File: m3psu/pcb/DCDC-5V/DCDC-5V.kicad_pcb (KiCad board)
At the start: 2 copper layers, 39.5 x 39.5 mm, 52 parts, among them IC1 LTC2975, IC2 TPS62133, IC3 TPS62152, J1 WEST TOP, J2 WEST BOT, J3 NORTH TOP, J4 EAST TOP, J5 EAST BOT, J6 NORTH BOT, Q1 NFET_GDS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

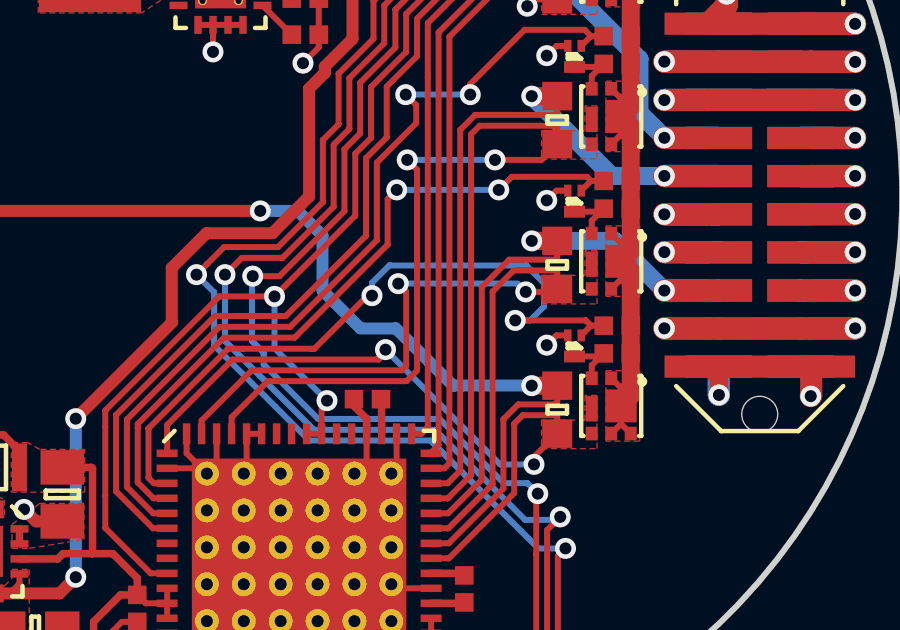
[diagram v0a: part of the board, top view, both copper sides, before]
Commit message: Small routing optimisation to DCDC-5V board
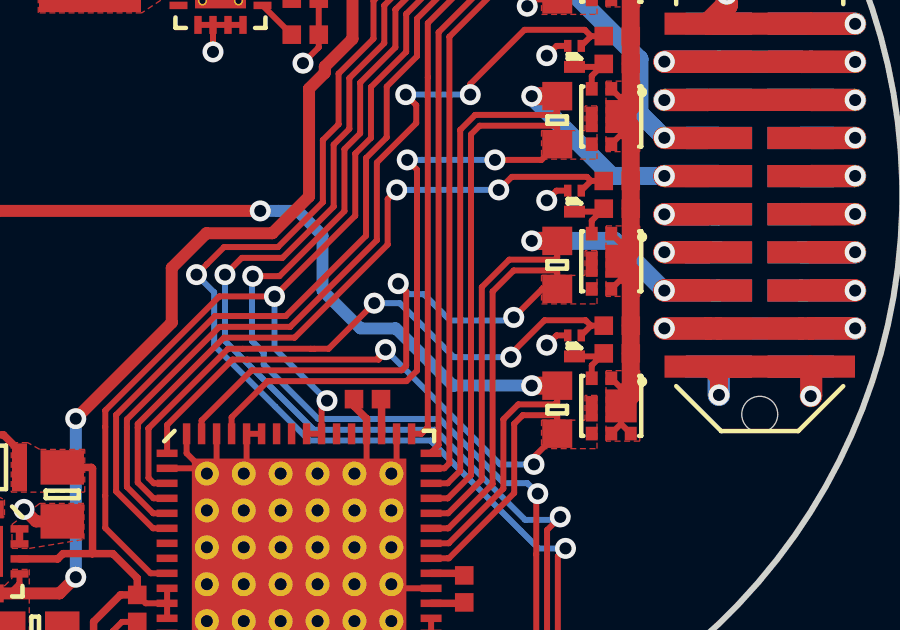
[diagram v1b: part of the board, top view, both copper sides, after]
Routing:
- net /VEN_0: track 23.7 -> 21.1 mm
- net /ISNS1+: track 28.4 -> 29.4 mm
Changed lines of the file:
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@@
     (thickness 1.6)
     (drawings 5)
-    (tracks 867)
+    (tracks 868)
     (zones 0)
     (modules 52)
@@
   )
   (setup
-    (last_trace_width 0.25)
+    (last_trace_width 0.2)
     (user_trace_width 0.16)
     (user_trace_width 0.2)
@@
   (segment (start 104.640655 112.105) (end 104.595 112.105) (width 0.2) (layer F.Cu) (net 41))
   (segment (start 104.595 112.105) (end 104.045 112.105) (width 0.2) (layer F.Cu) (net 41))
-  (segment (start 102.075 103.35) (end 102.075 102.922198) (width 0.2) (layer B.Cu) (net 42))
-  (segment (start 102.075 102.922198) (end 102.657199 102.339999) (width 0.2) (layer B.Cu) (net 42))
-  (segment (start 102.657199 102.339999) (end 107.217801 102.339999) (width 0.2) (layer B.Cu) (net 42))
-  (segment (start 107.217801 102.339999) (end 107.810001 102.932199) (width 0.2) (layer B.Cu) (net 42))
-  (segment (start 107.810001 102.932199) (end 107.810001 103.709973) (width 0.2) (layer B.Cu) (net 42))
-  (segment (start 107.810001 103.709973) (end 107.344974 104.175) (width 0.2) (layer B.Cu) (net 42))
-  (segment (start 107.344974 104.175) (end 106.85 104.175) (width 0.2) (layer B.Cu) (net 42))
+  (segment (start 103 103.6) (end 104.8 105.4) (width 0.2) (layer B.Cu) (net 42))
+  (segment (start 104.8 105.4) (end 106.705041 105.4) (width 0.2) (layer B.Cu) (net 42))
+  (segment (start 102.15 103.6) (end 103 103.6) (width 0.2) (layer B.Cu) (net 42))
+  (segment (start 100.15503 105.11997) (end 100.63003 105.11997) (width 0.2) (layer F.Cu) (net 42))
+  (segment (start 100.63003 105.11997) (end 102.15 103.6) (width 0.2) (layer F.Cu) (net 42))
+  (via (at 102.15 103.6) (size 0.7) (drill 0.4) (layers F.Cu B.Cu) (net 42))
+  (segment (start 109.195301 104.170301) (end 107.826897 104.170301) (width 0.2) (layer F.Cu) (net 42))
+  (segment (start 107.826897 104.170301) (end 106.705041 105.292157) (width 0.2) (layer F.Cu) (net 42))
+  (segment (start 106.705041 105.292157) (end 106.705041 105.4) (width 0.2) (layer F.Cu) (net 42))
+  (via (at 106.705041 105.4) (size 0.7) (drill 0.4) (layers F.Cu B.Cu) (net 42))
+  (segment (start 94.801998 109.605) (end 94.625 109.428002) (width 0.2) (layer F.Cu) (net 42))
+  (segment (start 95.245 109.605) (end 94.801998 109.605) (width 0.2) (layer F.Cu) (net 42))
+  (segment (start 94.625 109.428002) (end 94.625 107.775) (width 0.2) (layer F.Cu) (net 42))
+  (segment (start 97.277897 105.11997) (end 97.768766 105.11997) (width 0.2) (layer F.Cu) (net 42))
+  (segment (start 94.625 107.772867) (end 97.277897 105.11997) (width 0.2) (layer F.Cu) (net 42))
+  (segment (start 94.625 107.775) (end 94.625 107.772867) (width 0.2) (layer F.Cu) (net 42))
+  (segment (start 97.768766 105.11997) (end 100.03003 105.11997) (width 0.2) (layer F.Cu) (net 42))
   (segment (start 100.03003 105.11997) (end 100.15503 105.11997) (width 0.2) (layer F.Cu) (net 42))
-  (segment (start 100.15503 105.11997) (end 101.925 103.35) (width 0.2) (layer F.Cu) (net 42))
-  (segment (start 101.925 103.35) (end 102.075 103.35) (width 0.2) (layer F.Cu) (net 42))
-  (via (at 102.075 103.35) (size 0.7) (drill 0.4) (layers F.Cu B.Cu) (net 42))
   (segment (start 109.195301 104.170301) (end 109.190602 104.175) (width 0.2) (layer F.Cu) (net 42))
-  (segment (start 109.190602 104.175) (end 106.85 104.175) (width 0.2) (layer F.Cu) (net 42))
-  (segment (start 97.768766 105.11997) (end 100.03003 105.11997) (width 0.2) (layer F.Cu) (net 42))
-  (segment (start 94.625 107.775) (end 94.625 107.772867) (width 0.2) (layer F.Cu) (net 42))
-  (segment (start 94.625 107.772867) (end 97.277897 105.11997) (width 0.2) (layer F.Cu) (net 42))
-  (segment (start 97.277897 105.11997) (end 97.768766 105.11997) (width 0.2) (layer F.Cu) (net 42))
   (segment (start 109.375 104.35) (end 109.195301 104.170301) (width 0.2) (layer F.Cu) (net 42))
-  (segment (start 106.854699 104.170301) (end 106.85 104.175) (width 0.2) (layer F.Cu) (net 42))
-  (via (at 106.85 104.175) (size 0.7) (drill 0.4) (layers F.Cu B.Cu) (net 42))
   (segment (start 109.8 104.35) (end 109.375 104.35) (width 0.2) (layer F.Cu) (net 42))
   (segment (start 109.375 104.35) (end 109.05 104.675) (width 0.2) (layer F.Cu) (net 42))
-  (segment (start 94.625 109.428002) (end 94.625 107.775) (width 0.2) (layer F.Cu) (net 42))
-  (segment (start 95.245 109.605) (end 94.801998 109.605) (width 0.2) (layer F.Cu) (net 42))
-  (segment (start 94.801998 109.605) (end 94.625 109.428002) (width 0.2) (layer F.Cu) (net 42))
   (segment (start 109.239999 99.389999) (end 106.735001 99.389999) (width 0.2) (layer F.Cu) (net 43))
   (segment (start 102.9 99.825) (end 103.394974 99.825) (width 0.2) (layer B.Cu) (net 43))
@@
   (segment (start 104.045 112.605) (end 105.08 112.605) (width 0.25) (layer F.Cu) (net 52))
   (segment (start 105.08 112.605) (end 105.15 112.675) (width 0.25) (layer F.Cu) (net 52))
-  (segment (start 107.2 103.225) (end 108.15 103.225) (width 0.2) (layer F.Cu) (net 53))
+  (segment (start 108.25 103.125) (end 107.75 103.125) (width 0.2) (layer F.Cu) (net 53))
+  (segment (start 107.75 103.125) (end 106.8 104.075) (width 0.2) (layer F.Cu) (net 53))
+  (segment (start 104.675 104.175) (end 106.7 104.175) (width 0.2) (layer B.Cu) (net 53))
+  (segment (start 106.7 104.175) (end 106.8 104.075) (width 0.2) (layer B.Cu) (net 53))
+  (via (at 106.8 104.075) (size 0.7) (drill 0.4) (layers F.Cu B.Cu) (net 53))
+  (segment (start 103.799999 103.299999) (end 104.675 104.175) (width 0.2) (layer B.Cu) (net 53))
+  (segment (start 102.95 102.95) (end 103.299999 103.299999) (width 0.2) (layer B.Cu) (net 53))
+  (segment (start 103.299999 103.299999) (end 103.799999 103.299999) (width 0.2) (layer B.Cu) (net 53))
   (segment (start 108.15 103.225) (end 108.25 103.125) (width 0.2) (layer F.Cu) (net 53))
-  (segment (start 102.95 102.95) (end 106.925 102.95) (width 0.2) (layer B.Cu) (net 53))
-  (segment (start 106.925 102.95) (end 107.2 103.225) (width 0.2) (layer B.Cu) (net 53))
-  (via (at 107.2 103.225) (size 0.7) (drill 0.4) (layers F.Cu B.Cu) (net 53))
   (segment (start 103.214961 105.685039) (end 103.214961 103.214961) (width 0.2) (layer F.Cu) (net 53))
   (segment (start 103.214961 103.214961) (end 102.95 102.95) (width 0.2) (layer F.Cu) (net 53))

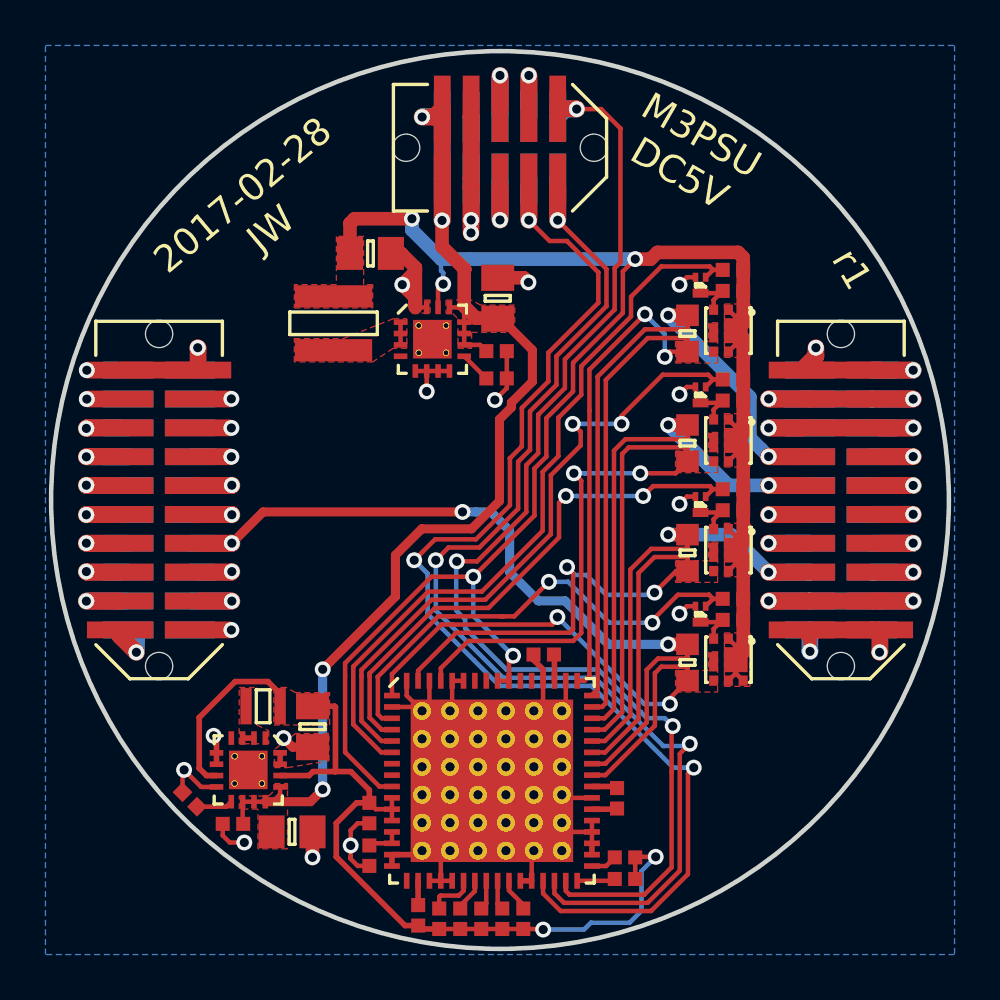
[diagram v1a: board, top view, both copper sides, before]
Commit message: Update NFET footprint on 5v board, add pull-downs
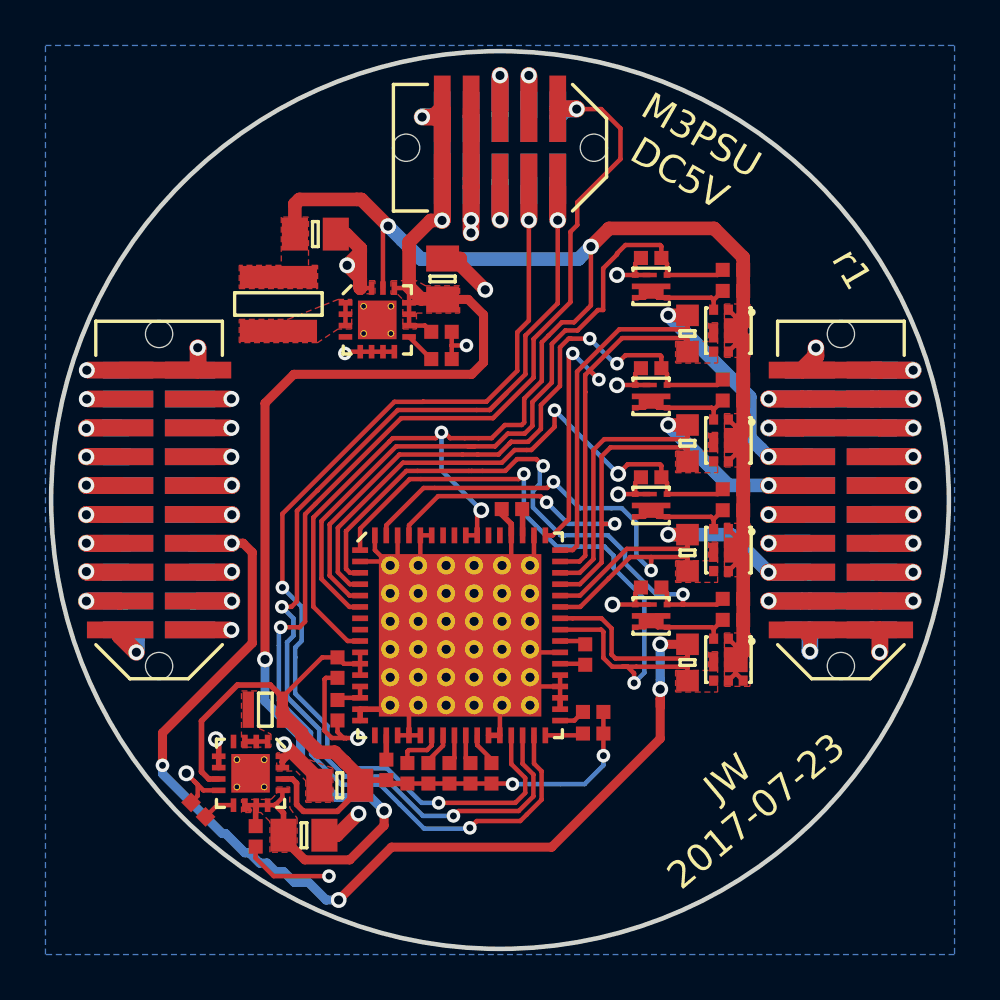
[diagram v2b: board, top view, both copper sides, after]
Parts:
- added R21: 1M, agg:0402, F.Cu at (106.7, 103.8)
- added R22: 1M, agg:0402, F.Cu at (106.7, 99.0)
- added R23: 1M, agg:0402, F.Cu at (106.7, 94.2)
- added R24: 1M, agg:0402, F.Cu at (106.7, 89.3)
- Q1, Q2, Q3, Q4: footprint agg:SOT-883-B -> agg:PowerPAK-SC-75-6L-Single
- moved G*** 35.0 mm to (65.0, 104.5)
- moved C1 6.55 mm to (92.8, 107.4)
- moved C3 6.55 mm to (92.8, 109.2)
- moved R1 6.55 mm to (95.0, 111.9)
- moved IC1 6.55 mm to (98.2, 106.0)
- moved R3 6.55 mm to (104.1, 109.3)
- moved R4 6.55 mm to (96.8, 112.0)
- moved R5 6.55 mm to (104.1, 110.3)
- moved R6 6.55 mm to (95.9, 112.0)
- moved R8 6.55 mm to (99.6, 112.0)
- moved C2 6.55 mm to (100.5, 100.4)
- moved R2 6.55 mm to (98.7, 112.0)
- moved R7 6.55 mm to (97.8, 112.0)
- moved C4 6.48 mm to (103.8, 106.8)
- moved C12 2.84 mm to (93.0, 112.5), turned to 180 degrees
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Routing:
- net /5v_CAN: track 35.5 -> 56.2 mm, vias 3 -> 5
- net /ISNS3+: track 40.7 -> 25.8 mm
- net VCC: track 54.5 -> 68.5 mm
- net /ISNS2+: track 36.3 -> 22.5 mm
- net GND: track 81.8 -> 95.4 mm
- net /SDA: track 54.2 -> 47.1 mm
- net /ISNS1+: track 29.4 -> 23.2 mm
- net /VEN_0: track 21.1 -> 27.0 mm
- net /ISNS0+: track 25.3 -> 30.5 mm
- net /5v_IMU: track 26.2 -> 21.1 mm
- net /5v_CAM: track 21.3 -> 16.3 mm
- net /5v_RADIO: track 31.7 -> 26.9 mm
- net 3v3: track 42.2 -> 37.6 mm
- net Net-(Q2-PadD): track 2.01 -> 6.45 mm
- net Net-(Q4-PadD): track 2.01 -> 6.44 mm
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- removed copper zone on F.Cu, net 3v3
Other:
- board text added: "JW 2017-07-23"
- board text removed: "2017-02-28 JW"

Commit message: Fix silkscreen, add test pads
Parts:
- added TP1: TESTPAD, agg:TESTPAD, F.Cu at (100.2, 91.6)
- added TP2: TESTPAD, agg:TESTPAD, F.Cu at (101.7, 90.3)
- added TP3: TESTPAD, agg:TESTPAD, F.Cu at (106.5, 86.8)
- added TP4: TESTPAD, agg:TESTPAD, F.Cu at (112.5, 90.2)
- C12, C8, C9: value 22µ -> 22u
- C5: value 10µ -> 10u
- L1: value 2µ2 -> 2u2
- L2: value 3µ3 -> 3u3
- moved G*** 35.2 mm to (99.9, 100.3)
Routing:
- net /~ALERT: track 57.0 -> 58.8 mm
- net GND: track 95.4 -> 96.6 mm, vias 24 -> 25
- net /SDA: track 47.1 -> 48.3 mm
- net /SCL: track 50.1 -> 51.0 mm
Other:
- board text added: "JW 2017-07-25"
- board text removed: "JW 2017-07-23"

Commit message: Add additional decoupling capacitor to 5V board
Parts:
- added C13: 22u, agg:0805, F.Cu at (111.6, 110.2)
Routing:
- net /V_DIST: track 89.8 -> 93.1 mm
- net GND: track 96.6 -> 95.5 mm, vias 25 -> 26
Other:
- board text added: "JW 2017-07-26"
- board text removed: "JW 2017-07-25"
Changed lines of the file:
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@@
 (kicad_pcb (version 20160815) (host pcbnew "(2016-12-10 revision 9c758c4)-makepkg")
   (general
-    (links 312)
-    (no_connects 0)
+    (links 314)
+    (no_connects 2)
     (area 80.149999 80.149999 119.850001 119.850001)
     (thickness 1.6)
@@
     (tracks 1026)
     (zones 0)
-    (modules 60)
+    (modules 61)
     (nets 67)
   )
@@
   )
   (setup
-    (last_trace_width 0.25)
+    (last_trace_width 0.6)
     (user_trace_width 0.16)
     (user_trace_width 0.2)
@@
       (net 1 GND))
   )
+  (module agg:0805 (layer F.Cu)
+    (at 111.6 110.175)
+    (fp_text reference C13 (at -2.425 0 90) (layer F.Fab)
+      (effects (font (size 1 1) (thickness 0.15)))
+    )
+    (fp_text value 22u (at 2.425 0 90) (layer F.Fab)
+      (effects (font (size 1 1) (thickness 0.15)))
+    )
+    (fp_line (start -1 -0.625) (end 1 -0.625) (layer F.Fab) (width 0.01))
+    (fp_line (start 1 -0.625) (end 1 0.625) (layer F.Fab) (width 0.01))
+    (fp_line (start 1 0.625) (end -1 0.625) (layer F.Fab) (width 0.01))
+    (fp_line (start -1 0.625) (end -1 -0.625) (layer F.Fab) (width 0.01))
+    (fp_line (start -0.5 -0.625) (end -0.5 0.625) (layer F.Fab) (width 0.01))
+    (fp_line (start 0.5 -0.625) (end 0.5 0.625) (layer F.Fab) (width 0.01))
+    (fp_line (start -0.125 -0.55) (end 0.125 -0.55) (layer F.SilkS) (width 0.15))
+    (fp_line (start 0.125 -0.55) (end 0.125 0.55) (layer F.SilkS) (width 0.15))
+    (fp_line (start 0.125 0.55) (end -0.125 0.55) (layer F.SilkS) (width 0.15))
+    (fp_line (start -0.125 0.55) (end -0.125 -0.55) (layer F.SilkS) (width 0.15))
+    (fp_line (start -1.75 -1) (end 1.75 -1) (layer F.CrtYd) (width 0.01))
+    (fp_line (start 1.75 -1) (end 1.75 1) (layer F.CrtYd) (width 0.01))
+    (fp_line (start 1.75 1) (end -1.75 1) (layer F.CrtYd) (width 0.01))
+    (fp_line (start -1.75 1) (end -1.75 -1) (layer F.CrtYd) (width 0.01))
+    (pad 1 smd rect (at -0.9 0) (size 1.15 1.45) (layers F.Cu F.Paste F.Mask)
+      (net 56 /V_DIST))
+    (pad 2 smd rect (at 0.9 0) (size 1.15 1.45) (layers F.Cu F.Paste F.Mask)
+      (net 1 GND))
+    (model ${KISYS3DMOD}/Resistors_SMD.3dshapes/R_0805.wrl
+      (at (xyz 0 0 0))
+      (scale (xyz 1 1 1))
+      (rotate (xyz 0 0 0))
+    )
+  )
   (gr_text r1 (at 115.3 89.775 300) (layer F.SilkS)
     (effects (font (size 1.2 1.2) (thickness 0.25)))
   )
-  (gr_text "JW\n2017-07-25" (at 110.8 112.75 40) (layer F.SilkS)
+  (gr_text "JW\n2017-07-26" (at 108.35 114.35 30) (layer F.SilkS)
     (effects (font (size 1.2 1.2) (thickness 0.25)))
   )
@@
   (gr_line (start 100 89) (end 100 120) (layer Dwgs.User) (width 0.2))
   (gr_circle (center 100 100) (end 119.75 100) (layer Edge.Cuts) (width 0.2))
+  (segment (start 112.5 110.175) (end 112.5 108.825) (width 0.6) (layer F.Cu) (net 1))
+  (via (at 112.5 108.825) (size 0.7) (drill 0.4) (layers F.Cu B.Cu) (net 1))
+  (segment (start 92.85 109.7) (end 92.34 109.7) (width 0.2) (layer F.Cu) (net 1))
+  (segment (start 92.34 109.7) (end 92.05 109.41) (width 0.2) (layer F.Cu) (net 1))
+  (segment (start 92.05 109.41) (end 92.05 108.749264) (width 0.2) (layer F.Cu) (net 1))
+  (segment (start 92.05 108.749264) (end 92.05 108.325) (width 0.2) (layer F.Cu) (net 1))
+  (segment (start 92.85 107.825) (end 92.55 107.825) (width 0.2) (layer F.Cu) (net 1))
+  (segment (start 92.55 107.825) (end 92.05 108.325) (width 0.2) (layer F.Cu) (net 1))
+  (via (at 92.05 108.325) (size 0.6) (drill 0.3) (layers F.Cu B.Cu) (net 1))
   (segment (start 112.525 90.225) (end 113.75 90.225) (width 0.2) (layer F.Cu) (net 1))
   (via (at 113.75 90.225) (size 0.6) (drill 0.3) (layers F.Cu B.Cu) (net 1))
@@
   (segment (start 92.05 112.3) (end 90.5 110.75) (width 0.6) (layer F.Cu) (net 1))
   (via (at 90.5 110.75) (size 0.7) (drill 0.4) (layers F.Cu B.Cu) (net 1))
-  (segment (start 92.6 110.475) (end 93.25 110.475) (width 0.2) (layer F.Cu) (net 1))
-  (segment (start 93.25 110.475) (end 93.75 110.475) (width 0.2) (layer F.Cu) (net 1))
-  (segment (start 92.85 109.7) (end 92.85 110.21) (width 0.2) (layer F.Cu) (net 1))
-  (segment (start 92.85 110.21) (end 93.115 110.475) (width 0.2) (layer F.Cu) (net 1))
-  (segment (start 93.115 110.475) (end 93.25 110.475) (width 0.2) (layer F.Cu) (net 1))
-  (segment (start 92.279999 110.154999) (end 92.6 110.475) (width 0.2) (layer F.Cu) (net 1))
-  (via (at 93.75 110.475) (size 0.7) (drill 0.4) (layers F.Cu B.Cu) (net 1))
-  (segment (start 92.279999 110.079999) (end 92.279999 110.154999) (width 0.2) (layer F.Cu) (net 1))
   (segment (start 86.949307 112.775693) (end 86.575 112.401386) (width 0.2) (layer F.Cu) (net 1))
   (segment (start 86.575 112.401386) (end 86.199307 112.025693) (width 0.2) (layer F.Cu) (net 1))
@@
   (segment (start 97.875 93.2) (end 98.525 93.2) (width 0.2) (layer F.Cu) (net 1))
   (via (at 98.525 93.2) (size 0.6) (drill 0.3) (layers F.Cu B.Cu) (net 1))
-  (segment (start 92.85 107.825) (end 92.34 107.825) (width 0.2) (layer F.Cu) (net 1))
-  (segment (start 92.34 107.825) (end 92.279999 107.885001) (width 0.2) (layer F.Cu) (net 1))
-  (segment (start 92.279999 107.885001) (end 92.279999 110.079999) (width 0.2) (layer F.Cu) (net 1))
   (segment (start 105.95 104.1) (end 106.2 103.85) (width 0.2) (layer F.Cu) (net 1))
   (segment (start 106.59 104.6) (end 105.95 104.6) (width 0.2) (layer F.Cu) (net 1))
@@
   (segment (start 103.75 102.45) (end 103.495 102.705) (width 0.2) (layer F.Cu) (net 55))
   (segment (start 103.495 102.705) (end 102.645 102.705) (width 0.2) (layer F.Cu) (net 55))
+  (segment (start 110.7 110.175) (end 110.7 107.35) (width 0.6) (layer F.Cu) (net 56))
+  (segment (start 110.7 107.35) (end 110.375 107.025) (width 0.6) (layer F.Cu) (net 56))
   (segment (start 104 88.85) (end 103.45 89.4) (width 0.6) (layer B.Cu) (net 56))
   (segment (start 103.45 89.4) (end 96.525 89.4) (width 0.6) (layer B.Cu) (net 56))
